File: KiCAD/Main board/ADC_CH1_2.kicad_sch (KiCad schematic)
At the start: 147 parts, among them K1 EA2-12NU, K2 EA2-12NU, Q1 BC847, Q2 BC847, Q3 BC847, Q4 BC857, U24 LM4562, U25 OPA1632DR, U34 TL072, U35 TL072, U36 LM339, U38 PGA2311P, U39 TXS0102, U4 OPA1632DR, U5 OPA1632DR, U6 LM4562, U7 PCM1804

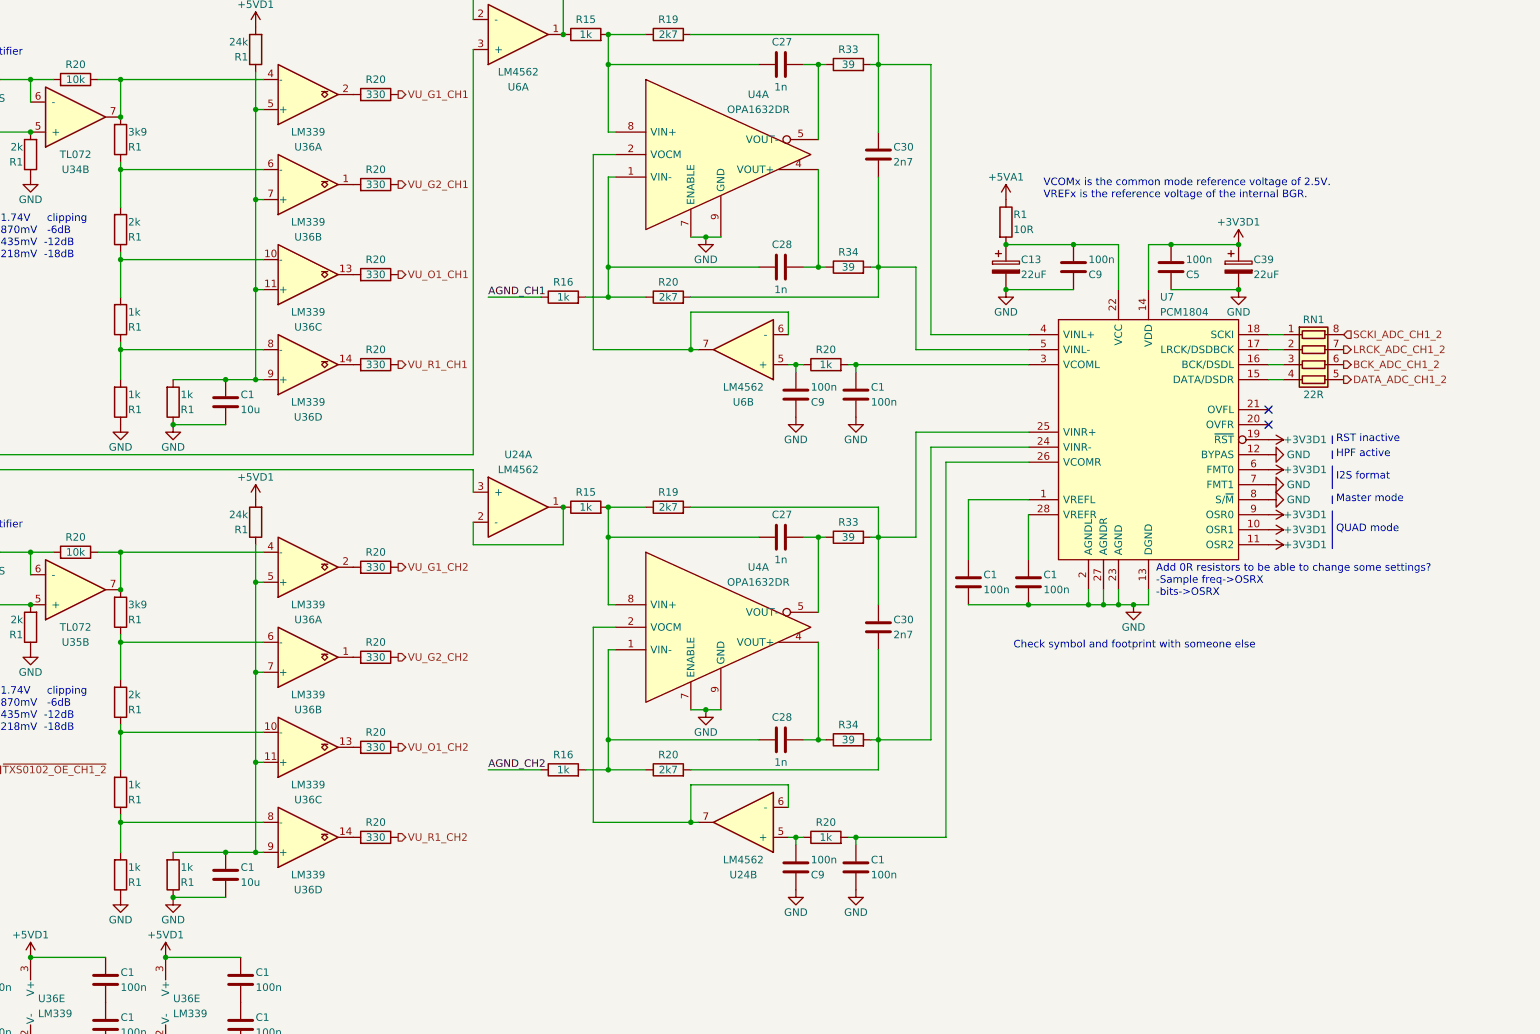
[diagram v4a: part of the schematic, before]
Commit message: Finalizer main board schematic exept passive order links. Schematic ready for review
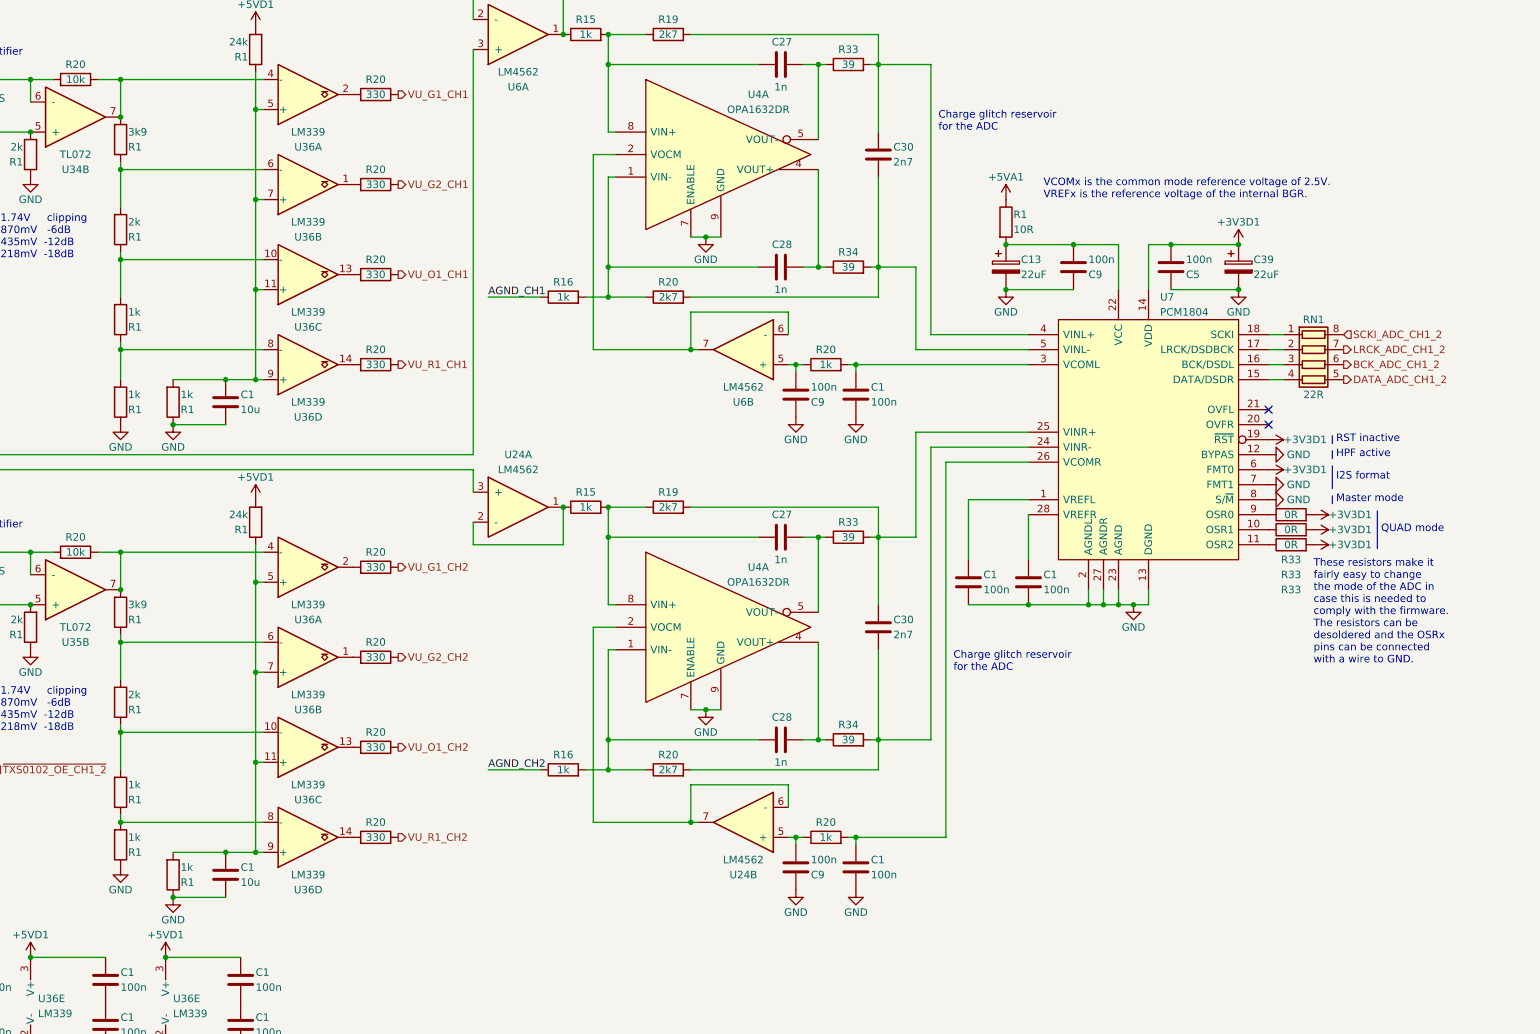
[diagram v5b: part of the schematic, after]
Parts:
- added R33 (x3): 0R, Resistor_SMD:R_0402_1005Metric, symbol Device:R
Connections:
- net +3V3D1: now also R33.2, R33.2, R33.2; no longer U7.10 (OSR1), U7.11 (OSR2), U7.9 (OSR0)
- new net: R33.1, U7.10 (OSR1)
- new net: R33.1, U7.11 (OSR2)
- new net: R33.1, U7.9 (OSR0)
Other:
- note added: "Charge glitch reservoir for the ADC"
- note added: "These resistors make it fairly easy to change the mode of the ADC in case this is needed to comply with the firmware. The resistors can be desoldered and the OSRx pins can be connected with a wire to GND."
- note removed: "Add 0R resistors to be able to change some settings? -Sample freq->OSRX -bits->OSRX"
- note removed: "Check symbol and footprint with someone else"
- moved on the sheet: R1
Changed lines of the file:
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@@
   (title_block
     (title "AUDIO-DSP_MAIN_BOARD")
+    (date "2023-06-06")
     (rev "R01")
   )
@@
     (stroke (width 0) (type default))
   )
-  (polyline (pts (xy 431.165 99.695) (xy 431.165 106.045))
+  (polyline (pts (xy 438.785 99.695) (xy 438.785 106.045))
     (stroke (width 0) (type default))
   )
@@
     (stroke (width 0) (type default))
   )
-  (wire (pts (xy 226.06 152.4) (xy 226.06 157.48))
-    (stroke (width 0) (type default))
-  )
   (wire (pts (xy 353.06 138.43) (xy 354.33 138.43))
     (stroke (width 0) (type default))
@@
     (stroke (width 0) (type default))
   )
-  (text "QUAD mode" (at 431.8 103.505 0)
+  (text "QUAD mode" (at 439.42 103.505 0)
     (effects (font (size 1.27 1.27)) (justify left bottom))
   )
@@
     (effects (font (size 1.27 1.27)) (justify left bottom))
   )
+  (text "Charge glitch reservoir\nfor the ADC" (at 364.49 35.56 0)
+    (effects (font (size 1.27 1.27)) (justify left bottom))
+  )
   (text "INPUT_SELECTOR_RELAY\nLOW=RCA\nHIGH-Jack" (at 132.08 43.18 0)
     (effects (font (size 1.27 1.27)) (justify left bottom))
@@
     (effects (font (size 1.27 1.27)) (justify left bottom))
   )
-  (text "Add 0R resistors to be able to change some settings?\n-Sample freq->OSRX\n-bits->OSRX"
-    (at 401.32 114.3 0)
-    (effects (font (size 1.27 1.27) (color 200 0 200 1)) (justify left bottom))
+  (text "These resistors make it\nfairly easy to change\nthe mode of the ADC in\ncase this is needed to\ncomply with the firmware.\nThe resistors can be\ndesoldered and the OSRx\npins can be connected\nwith a wire to GND."
+    (at 427.99 125.73 0)
+    (effects (font (size 1.27 1.27)) (justify left bottom))
   )
   (text "Unmuted" (at 137.16 100.965 0)
@@
     (effects (font (size 1.27 1.27)) (justify left bottom))
   )
+  (text "Charge glitch reservoir\nfor the ADC" (at 367.03 127 0)
+    (effects (font (size 1.27 1.27)) (justify left bottom))
+  )
   (text "Place this isolation\nresistors as close to\nthe audio signal\nas possible."
     (at 168.91 55.88 0)
@@
     (effects (font (size 1.27 1.27)) (justify left bottom))
   )
-  (text "Check symbol and footprint with someone else" (at 377.19 123.19 0)
-    (effects (font (size 1.27 1.27) (color 200 0 200 1)) (justify left bottom))
-  )
   (text "1.74V     clipping\n870mV   -6dB\n435mV  -12dB\n218mV  -18dB"
     (at 205.74 137.16 0)
@@
     )
   )
+  (symbol (lib_id "Device:R") (at 424.18 102.87 90) (unit 1)
+    (in_bom yes) (on_board yes) (dnp no)
+    (property "Reference" "R33" (at 424.18 110.49 90)
+      (effects (font (size 1.27 1.27)))
+    )
+    (property "Value" "0R" (at 424.18 102.87 90)
+      (effects (font (size 1.27 1.27)))
+    )
+    (property "Footprint" "Resistor_SMD:R_0402_1005Metric" (at 424.18 104.648 90)
+      (effects (font (size 1.27 1.27)) hide)
+    )
+    (property "Datasheet" "~" (at 424.18 102.87 0)
+      (effects (font (size 1.27 1.27)) hide)
+    )
+    (pin "1")
+    (pin "2")
+    (instances
+      (project "Main board"
+        (path "/2f8cbac6-fd11-4240-8e40-3bb6952a0324/03c234da-ad6d-41dc-b0ec-5880e5376fd2"
+          (reference "R33") (unit 1)
+        )
+        (path "/2f8cbac6-fd11-4240-8e40-3bb6952a0324/4e10d7ae-7c54-4ac5-ac67-e4842ffdf025"
+          (reference "R125") (unit 1)
+        )
+      )
+    )
+  )
   (symbol (lib_id "Device:R_Pack04") (at 427.99 74.93 270) (unit 1)
     (in_bom yes) (on_board yes) (dnp no)
@@
     )
   )
+  (symbol (lib_id "Device:R") (at 424.18 105.41 90) (unit 1)
+    (in_bom yes) (on_board yes) (dnp no)
+    (property "Reference" "R33" (at 424.18 113.03 90)
+      (effects (font (size 1.27 1.27)))
+    )
+    (property "Value" "0R" (at 424.18 105.41 90)
+      (effects (font (size 1.27 1.27)))
+    )
+    (property "Footprint" "Resistor_SMD:R_0402_1005Metric" (at 424.18 107.188 90)
+      (effects (font (size 1.27 1.27)) hide)
+    )
+    (property "Datasheet" "~" (at 424.18 105.41 0)
+      (effects (font (size 1.27 1.27)) hide)
+    )
+    (pin "1")
+    (pin "2")
+    (instances
+      (project "Main board"
+        (path "/2f8cbac6-fd11-4240-8e40-3bb6952a0324/03c234da-ad6d-41dc-b0ec-5880e5376fd2"
+          (reference "R33") (unit 1)
+        )
+        (path "/2f8cbac6-fd11-4240-8e40-3bb6952a0324/4e10d7ae-7c54-4ac5-ac67-e4842ffdf025"
+          (reference "R181") (unit 1)
+        )
+      )
+    )
+  )
   (symbol (lib_id "power:GND") (at 233.68 190.5 0) (unit 1)
     (in_bom yes) (on_board yes) (dnp no)
@@
     )
   )
-  (symbol (lib_id "Audio_DSP:+3V3D1") (at 420.37 105.41 270) (unit 1)
+  (symbol (lib_id "Audio_DSP:+3V3D1") (at 427.99 105.41 270) (unit 1)
     (in_bom no) (on_board no) (dnp no)
-    (property "Reference" "#PWR0100" (at 417.83 105.41 0)
+    (property "Reference" "#PWR0100" (at 425.45 105.41 0)
       (effects (font (size 1.27 1.27)) hide)
     )
-    (property "Value" "+3V3D1" (at 422.91 105.41 90)
+    (property "Value" "+3V3D1" (at 430.53 105.41 90)
       (effects (font (size 1.27 1.27)) (justify left))
     )
-    (property "Footprint" "" (at 420.37 105.41 0)
+    (property "Footprint" "" (at 427.99 105.41 0)
       (effects (font (size 1.27 1.27)) hide)
     )
-    (property "Datasheet" "" (at 420.37 105.41 0)
+    (property "Datasheet" "" (at 427.99 105.41 0)
       (effects (font (size 1.27 1.27)) hide)
     )
@@
     )
   )
-  (symbol (lib_id "power:GND") (at 226.06 165.1 0) (unit 1)
+  (symbol (lib_id "power:GND") (at 226.06 160.02 0) (unit 1)
     (in_bom yes) (on_board yes) (dnp no)
-    (property "Reference" "#PWR0117" (at 226.06 171.45 0)
+    (property "Reference" "#PWR0117" (at 226.06 166.37 0)
       (effects (font (size 1.27 1.27)) hide)
     )
-    (property "Value" "GND" (at 226.06 168.91 0)
+    (property "Value" "GND" (at 226.06 163.83 0)
       (effects (font (size 1.27 1.27)))
     )
-    (property "Footprint" "" (at 226.06 165.1 0)
+    (property "Footprint" "" (at 226.06 160.02 0)
       (effects (font (size 1.27 1.27)) hide)
     )
-    (property "Datasheet" "" (at 226.06 165.1 0)
+    (property "Datasheet" "" (at 226.06 160.02 0)
       (effects (font (size 1.27 1.27)) hide)
     )
@@
     )
   )
-  (symbol (lib_id "Audio_DSP:+3V3D1") (at 420.37 100.33 270) (unit 1)
+  (symbol (lib_id "Audio_DSP:+3V3D1") (at 427.99 100.33 270) (unit 1)
     (in_bom no) (on_board no) (dnp no)
-    (property "Reference" "#PWR0100" (at 417.83 100.33 0)
+    (property "Reference" "#PWR0100" (at 425.45 100.33 0)
       (effects (font (size 1.27 1.27)) hide)
     )
-    (property "Value" "+3V3D1" (at 422.91 100.33 90)
+    (property "Value" "+3V3D1" (at 430.53 100.33 90)
       (effects (font (size 1.27 1.27)) (justify left))
     )
-    (property "Footprint" "" (at 420.37 100.33 0)
+    (property "Footprint" "" (at 427.99 100.33 0)
       (effects (font (size 1.27 1.27)) hide)
     )
-    (property "Datasheet" "" (at 420.37 100.33 0)
+    (property "Datasheet" "" (at 427.99 100.33 0)
       (effects (font (size 1.27 1.27)) hide)
     )
@@
     )
   )
-  (symbol (lib_id "Device:R") (at 226.06 161.29 0) (mirror x) (unit 1)
+  (symbol (lib_id "Device:R") (at 226.06 156.21 0) (mirror x) (unit 1)
     (in_bom yes) (on_board yes) (dnp no)
-    (property "Reference" "R1" (at 227.33 162.56 0)
+    (property "Reference" "R1" (at 227.33 157.48 0)
       (effects (font (size 1.27 1.27)) (justify left))
     )
-    (property "Value" "1k" (at 227.33 160.02 0)
+    (property "Value" "1k" (at 227.33 154.94 0)
       (effects (font (size 1.27 1.27)) (justify left))
     )
-    (property "Footprint" "Resistor_SMD:R_0805_2012Metric" (at 224.282 161.29 90)
+    (property "Footprint" "Resistor_SMD:R_0805_2012Metric" (at 224.282 156.21 90)
       (effects (font (size 1.27 1.27)) hide)
     )
-    (property "Datasheet" "~" (at 226.06 161.29 0)
+    (property "Datasheet" "~" (at 226.06 156.21 0)
       (effects (font (size 1.27 1.27)) hide)
     )
@@
     )
   )
+  (symbol (lib_id "Device:R") (at 424.18 100.33 90) (unit 1)
+    (in_bom yes) (on_board yes) (dnp no)
+    (property "Reference" "R33" (at 424.18 107.95 90)
+      (effects (font (size 1.27 1.27)))
+    )
+    (property "Value" "0R" (at 424.18 100.33 90)
+      (effects (font (size 1.27 1.27)))
+    )
+    (property "Footprint" "Resistor_SMD:R_0402_1005Metric" (at 424.18 102.108 90)
+      (effects (font (size 1.27 1.27)) hide)
+    )
+    (property "Datasheet" "~" (at 424.18 100.33 0)
+      (effects (font (size 1.27 1.27)) hide)
+    )
+    (pin "1")
+    (pin "2")
+    (instances
+      (project "Main board"
+        (path "/2f8cbac6-fd11-4240-8e40-3bb6952a0324/03c234da-ad6d-41dc-b0ec-5880e5376fd2"
+          (reference "R33") (unit 1)
+        )
+        (path "/2f8cbac6-fd11-4240-8e40-3bb6952a0324/4e10d7ae-7c54-4ac5-ac67-e4842ffdf025"
+          (reference "R124") (unit 1)
+        )
+      )
+    )
+  )
   (symbol (lib_id "Transistor_BJT:BC847") (at 54.61 46.99 0) (mirror y) (unit 1)
     (in_bom yes) (on_board yes) (dnp no) (fields_autoplaced)
@@
     )
   )
-  (symbol (lib_id "Audio_DSP:+3V3D1") (at 420.37 102.87 270) (unit 1)
+  (symbol (lib_id "Audio_DSP:+3V3D1") (at 427.99 102.87 270) (unit 1)
     (in_bom no) (on_board no) (dnp no)
-    (property "Reference" "#PWR0100" (at 417.83 102.87 0)
+    (property "Reference" "#PWR0100" (at 425.45 102.87 0)
       (effects (font (size 1.27 1.27)) hide)
     )
-    (property "Value" "+3V3D1" (at 422.91 102.87 90)
+    (property "Value" "+3V3D1" (at 430.53 102.87 90)
       (effects (font (size 1.27 1.27)) (justify left))
     )
-    (property "Footprint" "" (at 420.37 102.87 0)
+    (property "Footprint" "" (at 427.99 102.87 0)
       (effects (font (size 1.27 1.27)) hide)
     )
-    (property "Datasheet" "" (at 420.37 102.87 0)
+    (property "Datasheet" "" (at 427.99 102.87 0)
       (effects (font (size 1.27 1.27)) hide)
     )

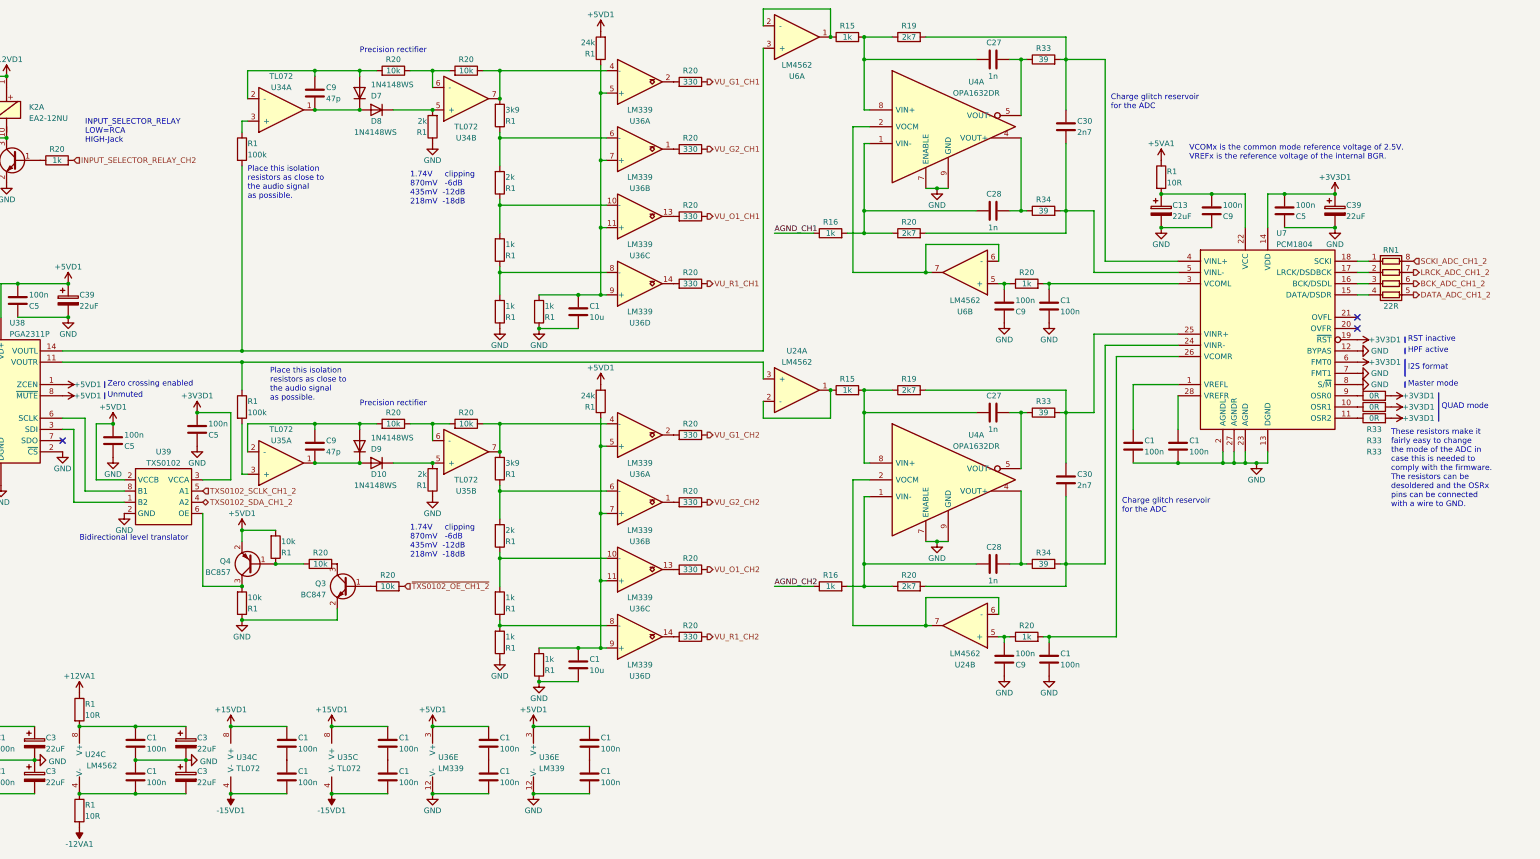
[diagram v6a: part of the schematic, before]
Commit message: Added component links
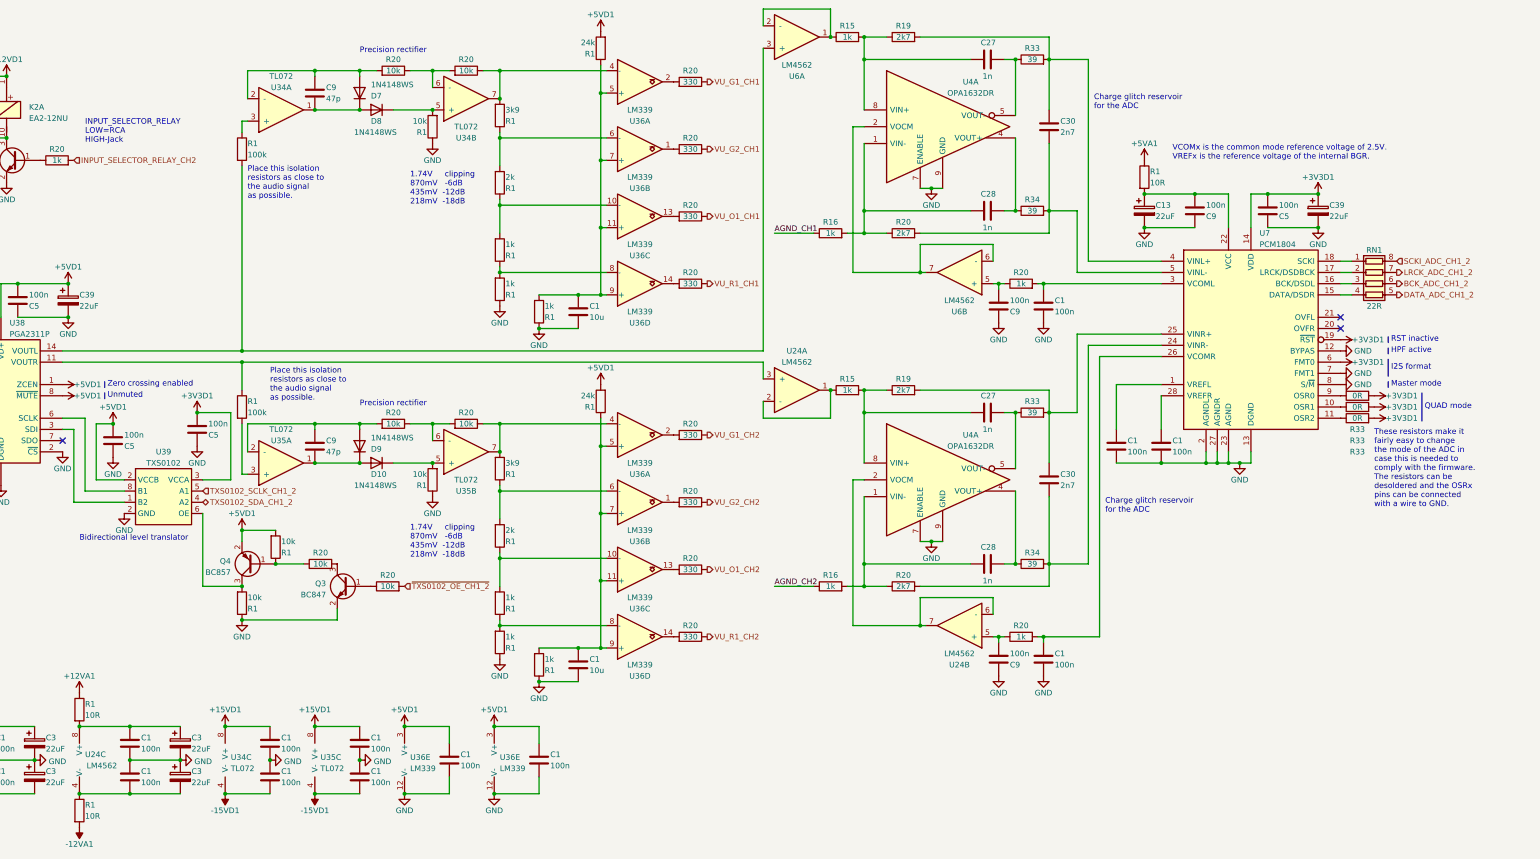
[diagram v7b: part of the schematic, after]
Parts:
- removed C1 (x2): 100n, Capacitor_SMD:C_0402_1005Metric, symbol Device:C
- R1: value 2k -> 10k
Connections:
- net GND: now also C1.1, C1.1, C1.2, C1.2, C1.2, C1.2
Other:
- moved on the sheet: C1, C13, C27, C28, C3, C30, C39, C5, C9, R1, R19, R20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
